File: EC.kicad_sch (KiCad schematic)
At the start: 3 parts, among them CN1 BM04B-SRSS-TB(LF)(SN), CN3 ZH1.5-6P-LT, J2 Conn_02x05_Odd_Even

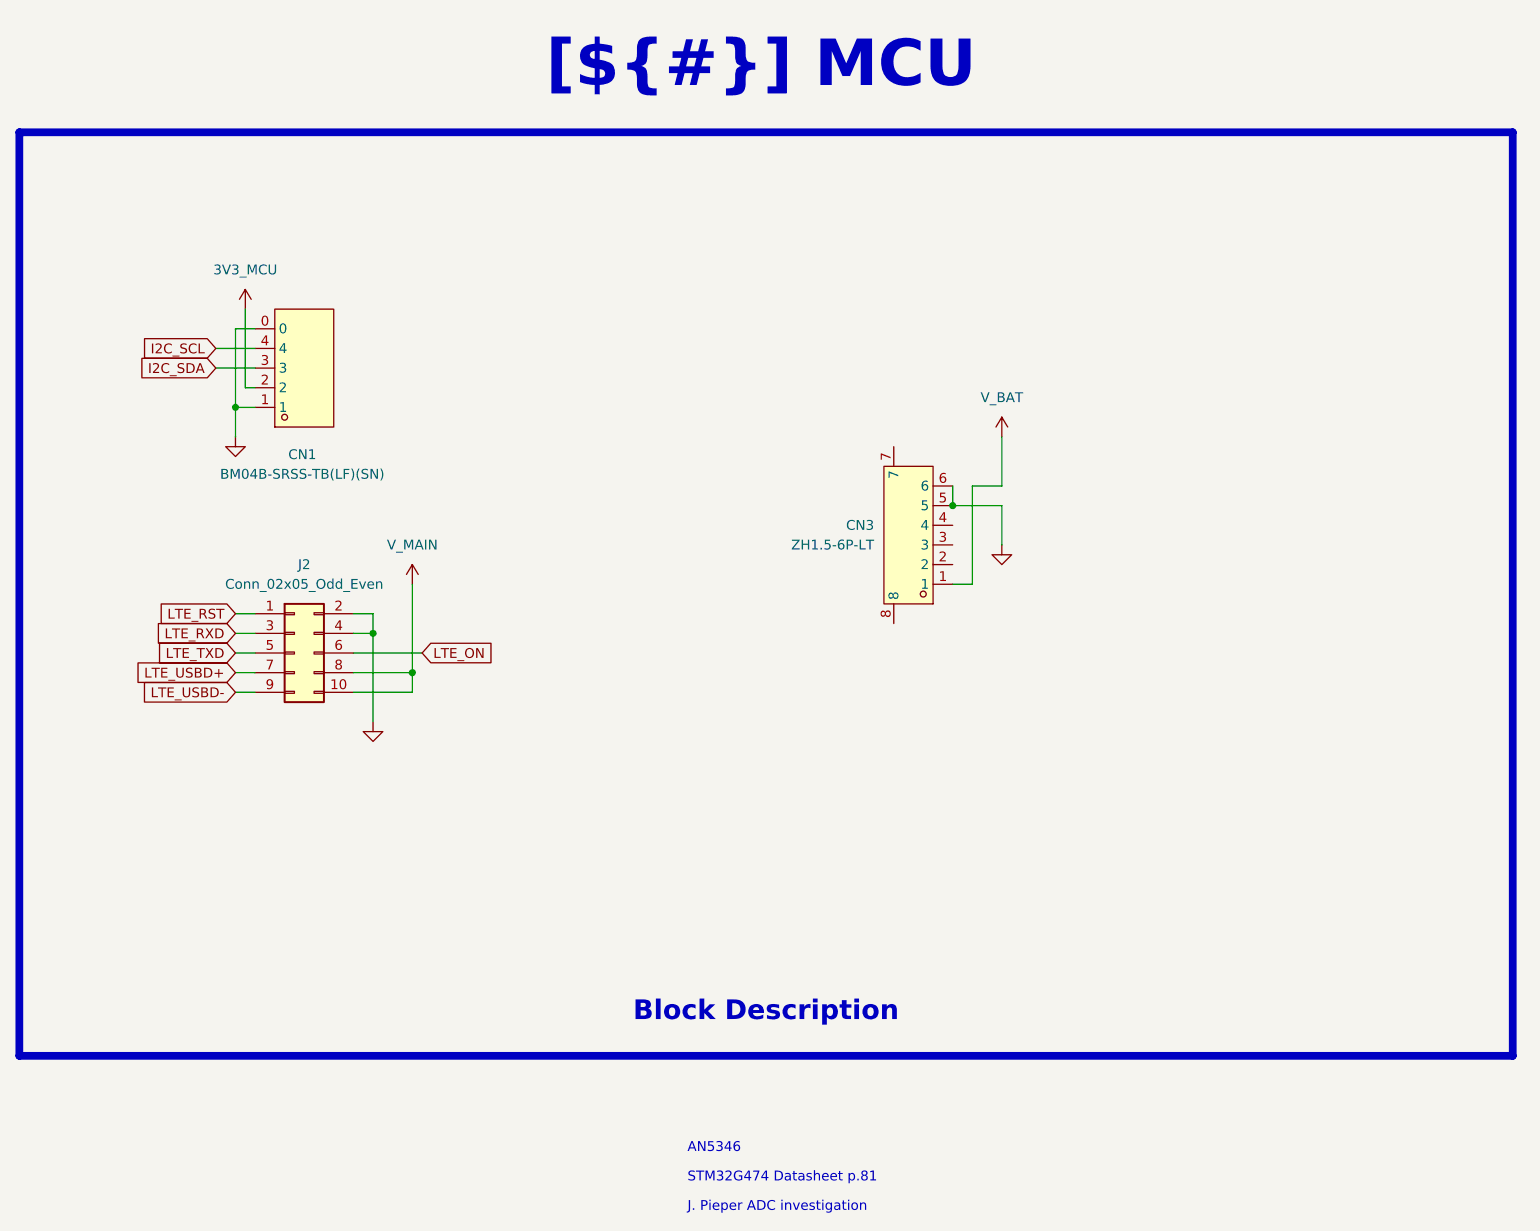
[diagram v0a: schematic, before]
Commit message: [Schematic][Added] Project Architecture, connectors
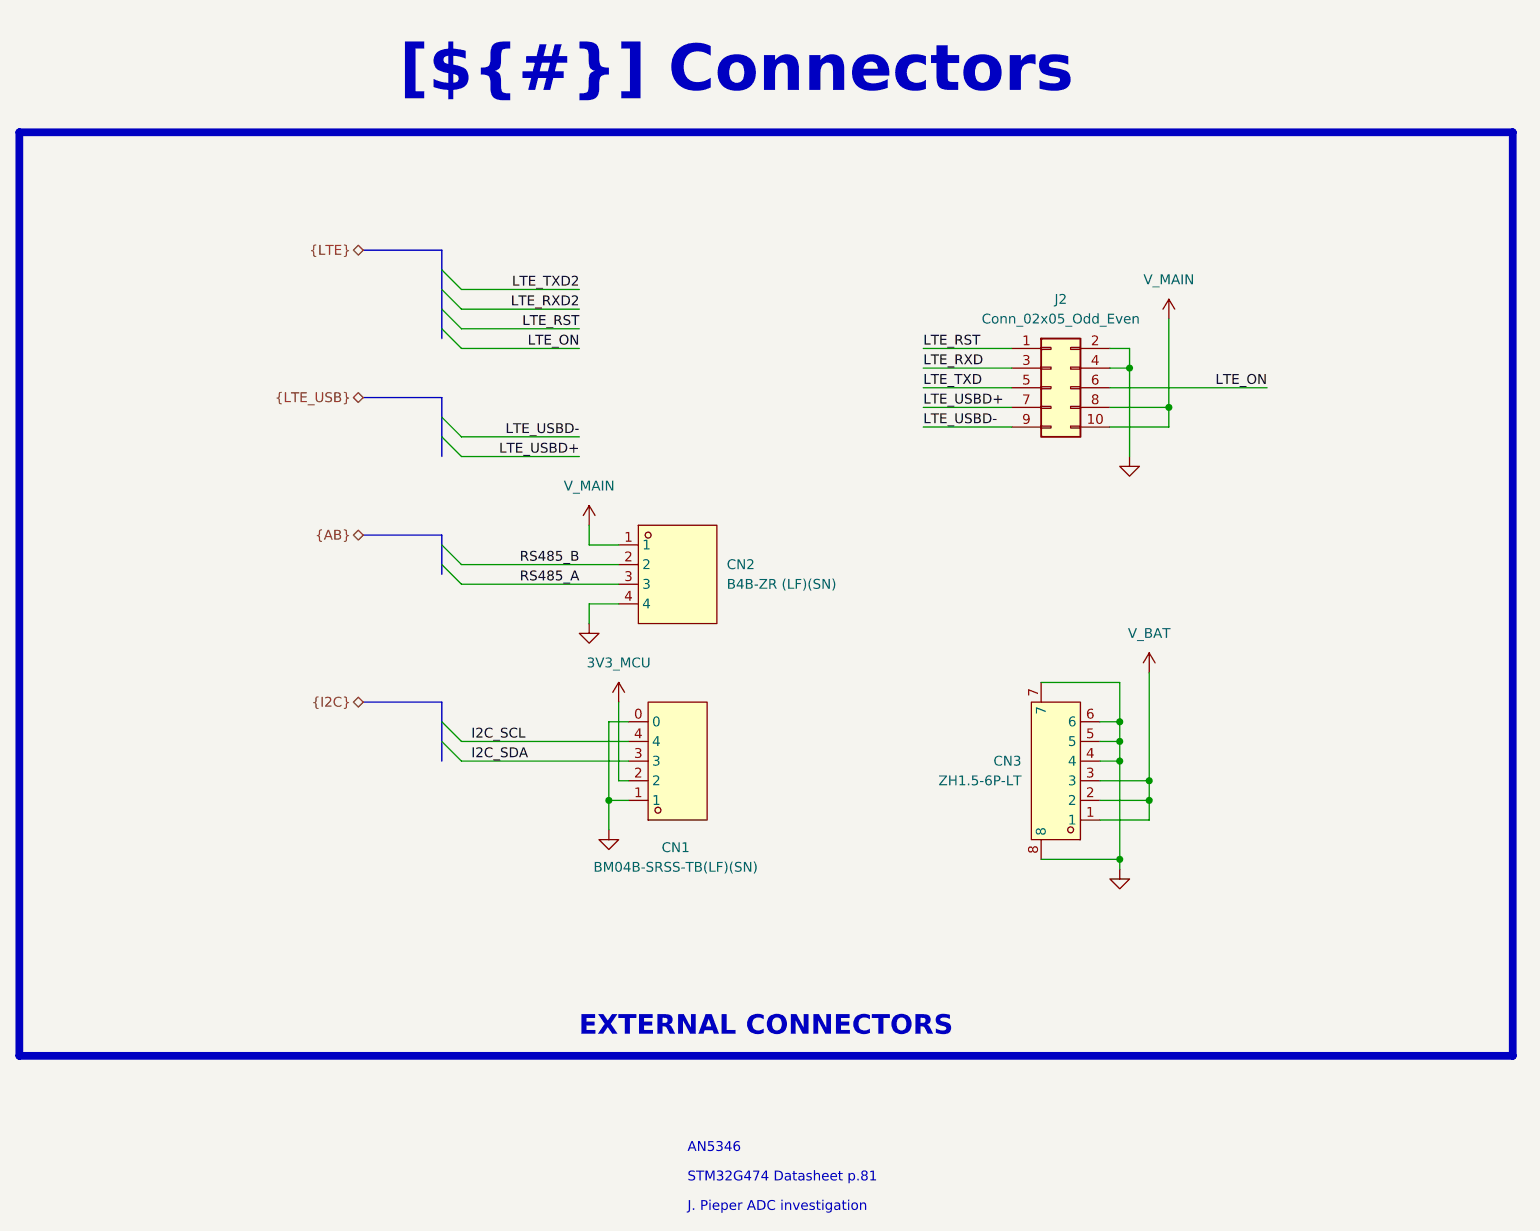
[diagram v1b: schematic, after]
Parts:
- added CN2: B4B-ZR (LF)(SN), easyeda2kicad:CONN-TH_B4B-ZR-LF-SN, symbol easyeda2kicad:B4B-ZR(LF)(SN)
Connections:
- net GND: now also CN3.4, CN3.7, CN3.8, CN2.4
- net V_BAT: now also CN3.2, CN3.3
- net V_MAIN: now also CN2.1
- new net RS485_A: CN2.3
- new net RS485_B: CN2.2
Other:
- title: MCU -> Connectors
- moved on the sheet: CN1, CN3, J2

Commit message: [Schematic][Added] Net labels
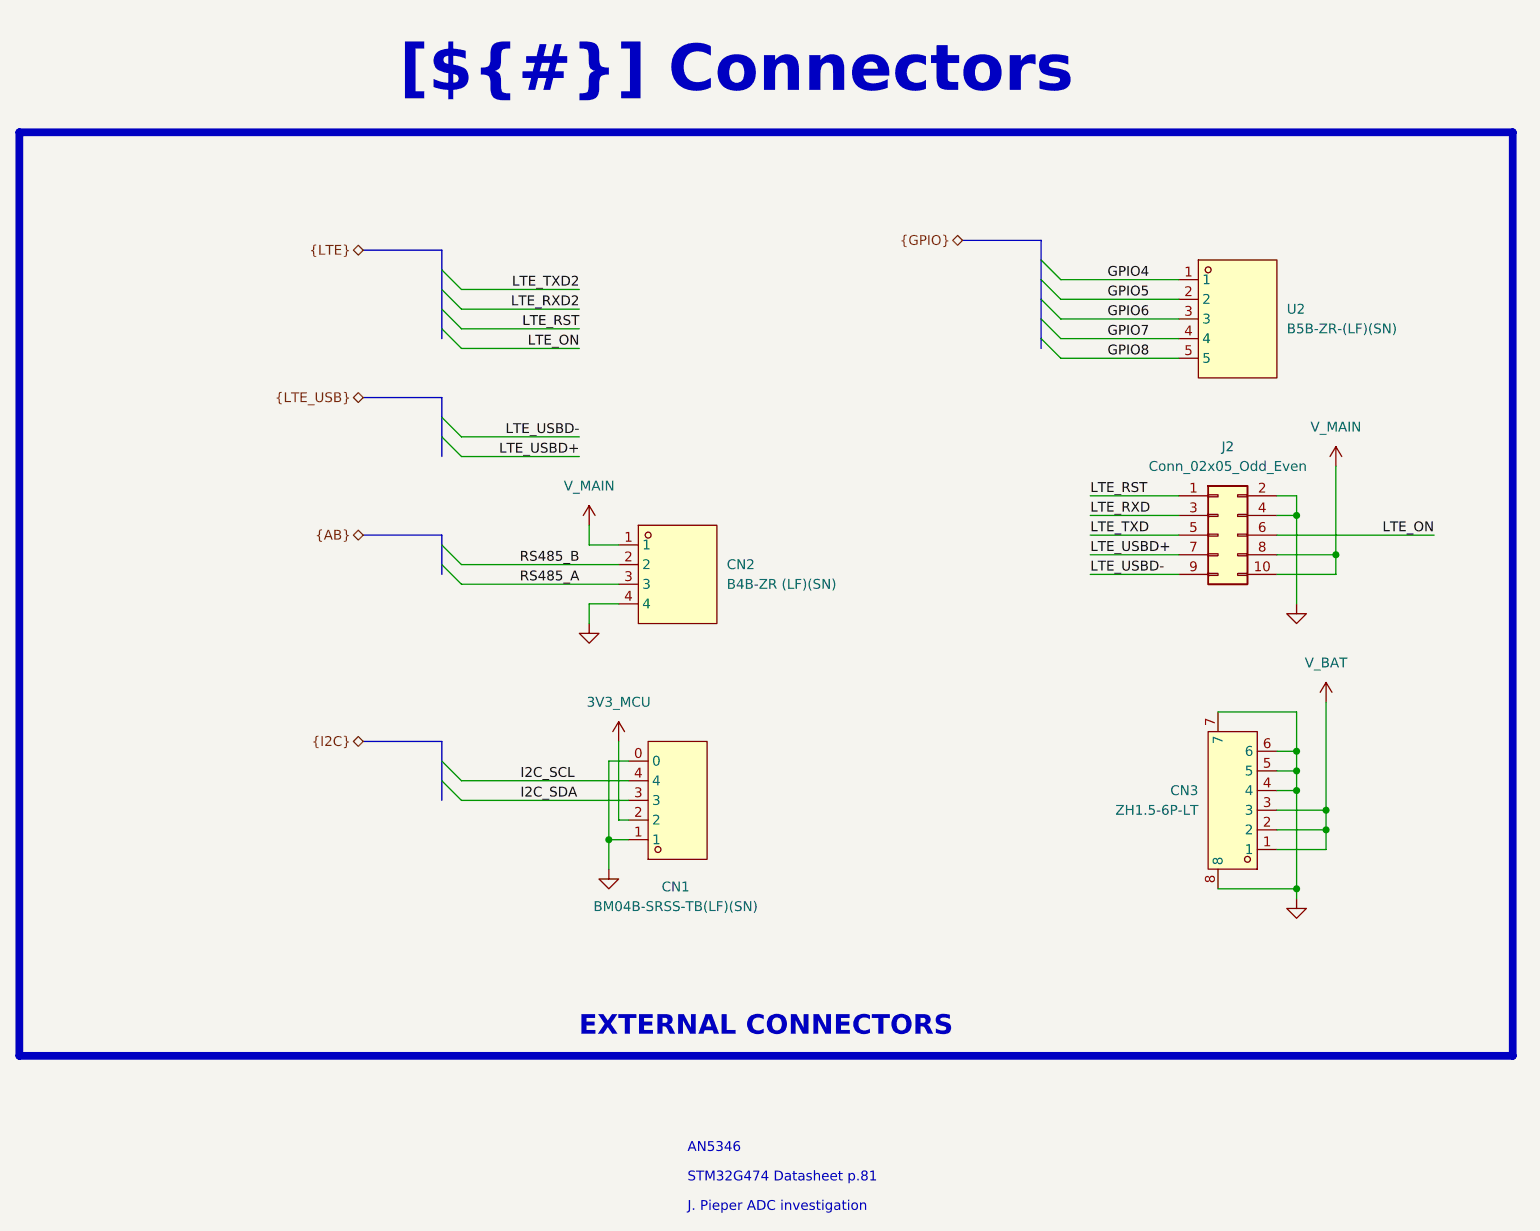
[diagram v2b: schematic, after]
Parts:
- added U2: B5B-ZR-(LF)(SN), easyeda2kicad:CONN-TH_5P-P1.50_B5B-ZR-LF-SN, symbol easyeda2kicad:B5B-ZR-(LF)(SN)
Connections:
- new net GPIO4: U2.1
- new net GPIO5: U2.2
- new net GPIO6: U2.3
- new net GPIO7: U2.4
- new net GPIO8: U2.5
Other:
- moved on the sheet: CN1, CN3, J2

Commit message: [PCB/SCH][Added] Preliminary version
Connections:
- net LTE_RXD is gone; now on net LTE_RXD2: J2.3 (Pin_3)
- net LTE_TXD is gone; now on net LTE_TXD2: J2.5 (Pin_5)
- net GND: now also CN3.1, CN3.2, CN3.3; no longer CN3.4, CN3.5, CN3.6
- net RS485_A: now also CN2.2; no longer CN2.3
- net RS485_B: now also CN2.3; no longer CN2.2
- net V_BAT: now also CN3.4, CN3.5, CN3.6; no longer CN3.1, CN3.2, CN3.3

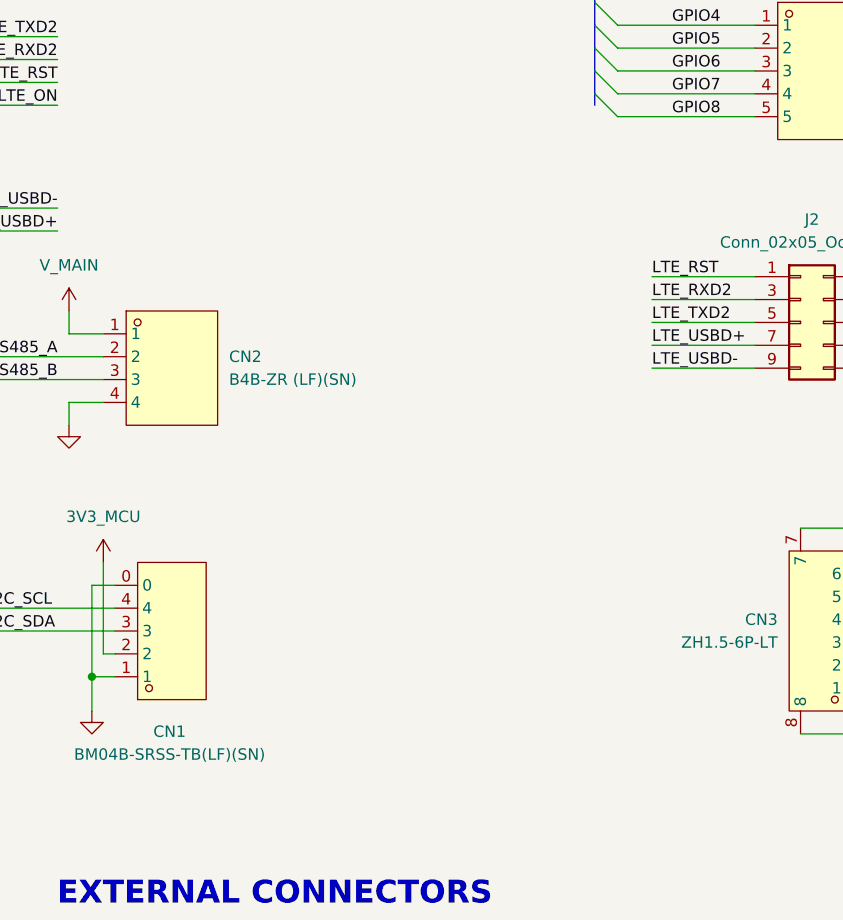
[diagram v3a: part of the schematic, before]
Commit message: [Schematic][Added] Connectors and first PCB layout
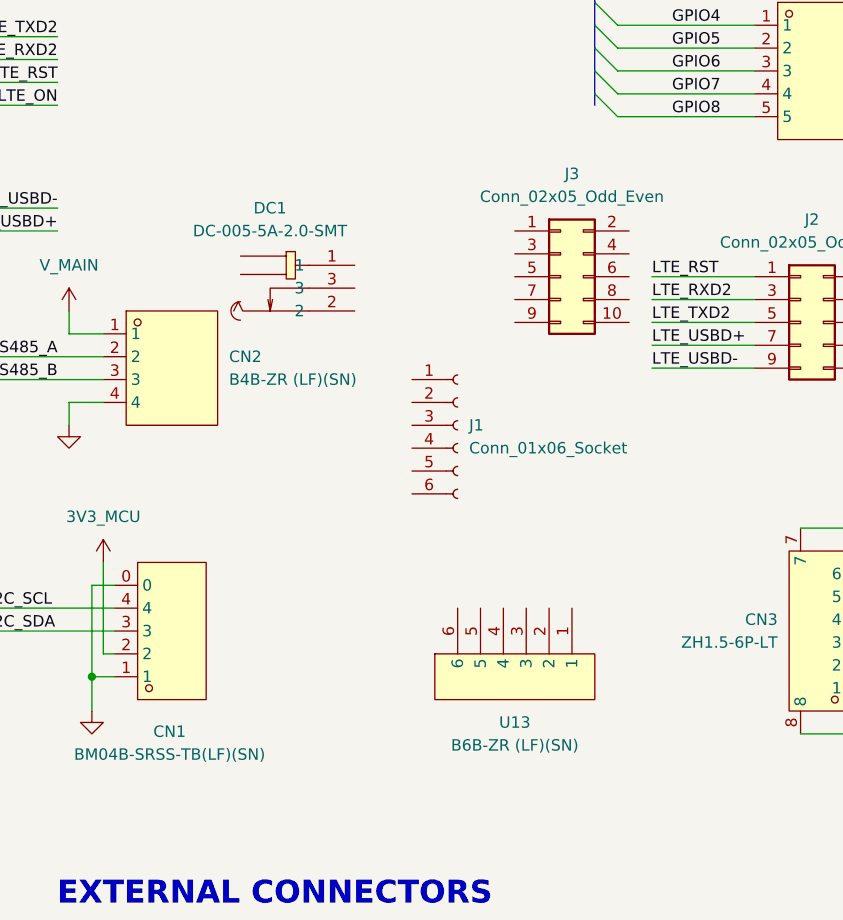
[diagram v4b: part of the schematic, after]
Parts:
- added DC1: DC-005-5A-2.0-SMT, easyeda2kicad:DC-IN-TH_DC-005-5A-2.0-SMT, symbol easyeda2kicad:DC-005-5A-2.0-SMT
- added J1: Conn_01x06_Socket, Connector_JST:JST_ZH_B6B-ZR_1x06_P1.50mm_Vertical, symbol Connector:Conn_01x06_Socket
- added J3: Conn_02x05_Odd_Even, Connector_PinHeader_2.54mm:PinHeader_2x05_P2.54mm_Vertical, symbol Connector_Generic:Conn_02x05_Odd_Even
- added U13: B6B-ZR (LF)(SN), easyeda2kicad:CONN-TH-6P-P1.50_B6B-ZR-LF-SN, symbol easyeda2kicad:B6B-ZR(LF)(SN)
